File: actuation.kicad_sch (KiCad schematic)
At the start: 0 parts

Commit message: GPIO, ADC
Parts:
- added U?: TLI4971, Package_SON:Infineon_PG-TISON-8-5, symbol actuation:TLI4971
- added U?: PCA9615, Package_SO:TSSOP-10_3x3mm_P0.5mm, symbol actuation:PCA9615
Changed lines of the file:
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@@
 (kicad_sch (version 20211123) (generator eeschema)
   (paper "A4")
+  (symbol (lib_id "actuation:TLI4971") (at 41.91 107.95 0) (unit 1)
+    (in_bom yes) (on_board yes) (fields_autoplaced)
+    (property "Reference" "U?" (id 0) (at 42.545 101.6 0))
+    (property "Value" "TLI4971" (id 1) (at 42.545 104.14 0))
+    (property "Footprint" "Package_SON:Infineon_PG-TISON-8-5" (id 2) (at 44.45 125.73 0)
+      (effects (font (size 1.27 1.27)) hide)
+    )
+    (property "Datasheet" "https://www.infineon.com/dgdl/Infineon-TLI4971_25_50_75_120-DataSheet-v01_20-EN.pdf?fileId=5546d462700c0ae6017034d731621b09" (id 3) (at 40.64 128.27 0)
+      (effects (font (size 1.27 1.27)) hide)
+    )
+    (property "MPN" "TLI4971A050T5UE0001XUMA1" (id 4) (at 44.45 123.19 0)
+      (effects (font (size 1.27 1.27)) hide)
+    )
+    (pin "1")
+    (pin "2")
+    (pin "3")
+    (pin "4")
+    (pin "5")
+    (pin "6")
+    (pin "7")
+    (pin "8")
+  )
+  (symbol (lib_id "actuation:PCA9615") (at 45.72 64.77 0) (unit 1)
+    (in_bom yes) (on_board yes) (fields_autoplaced)
+    (property "Reference" "U?" (id 0) (at 45.72 59.69 0))
+    (property "Value" "PCA9615" (id 1) (at 45.72 62.23 0))
+    (property "Footprint" "Package_SO:TSSOP-10_3x3mm_P0.5mm" (id 2) (at 45.72 90.17 0)
+      (effects (font (size 1.27 1.27)) hide)
+    )
+    (property "Datasheet" "https://www.nxp.com/docs/en/data-sheet/PCA9615.pdf" (id 3) (at 46.99 95.25 0)
+      (effects (font (size 1.27 1.27)) hide)
+    )
+    (property "MPN" "PCA9615DPZ" (id 4) (at 45.72 92.71 0)
+      (effects (font (size 1.27 1.27)) hide)
+    )
+    (pin "1")
+    (pin "10")
+    (pin "2")
+    (pin "3")
+    (pin "4")
+    (pin "5")
+    (pin "6")
+    (pin "7")
+    (pin "8")
+    (pin "9")
+  )
   (sheet_instances
     (path "/" (page "1"))
   )
+  (symbol_instances
+    (path "/1d4e175b-070d-4ba2-acb6-e76800f88675"
+      (reference "U?") (unit 1) (value "TLI4971") (footprint "Package_SON:Infineon_PG-TISON-8-5")
+    )
+    (path "/b052b9a3-1f94-4103-824a-f8b60996bb3f"
+      (reference "U?") (unit 1) (value "PCA9615") (footprint "Package_SO:TSSOP-10_3x3mm_P0.5mm")
+    )
+  )
 )

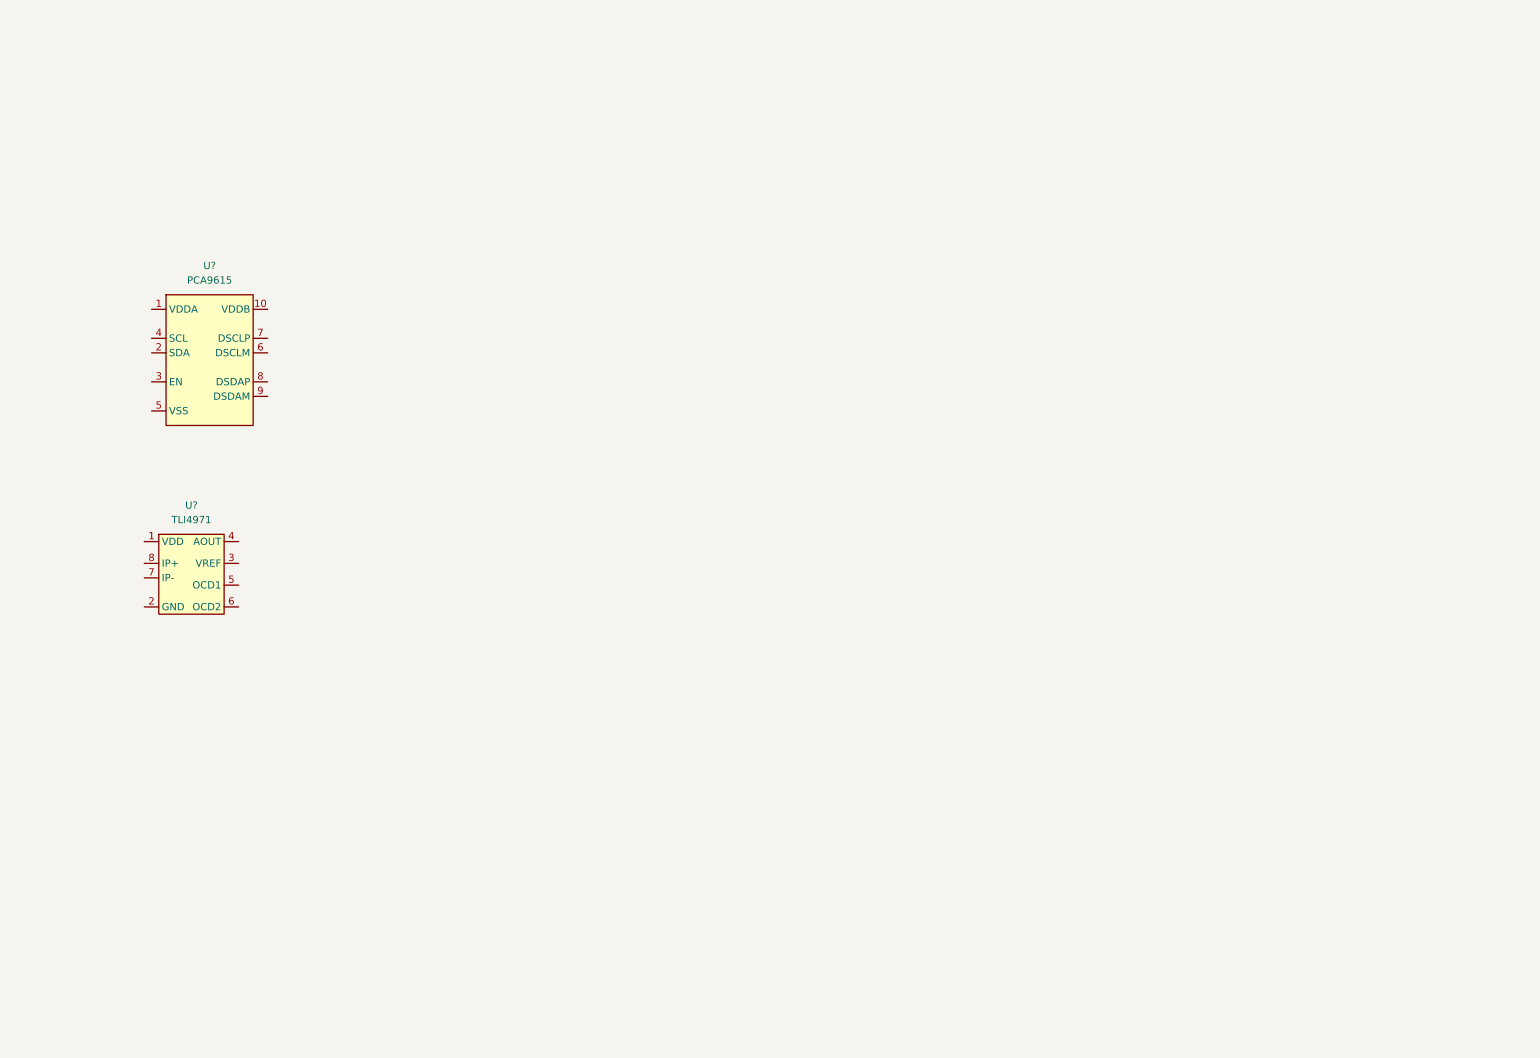
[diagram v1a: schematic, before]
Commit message: made symbols for ssr, optocoupler (missing footprint)
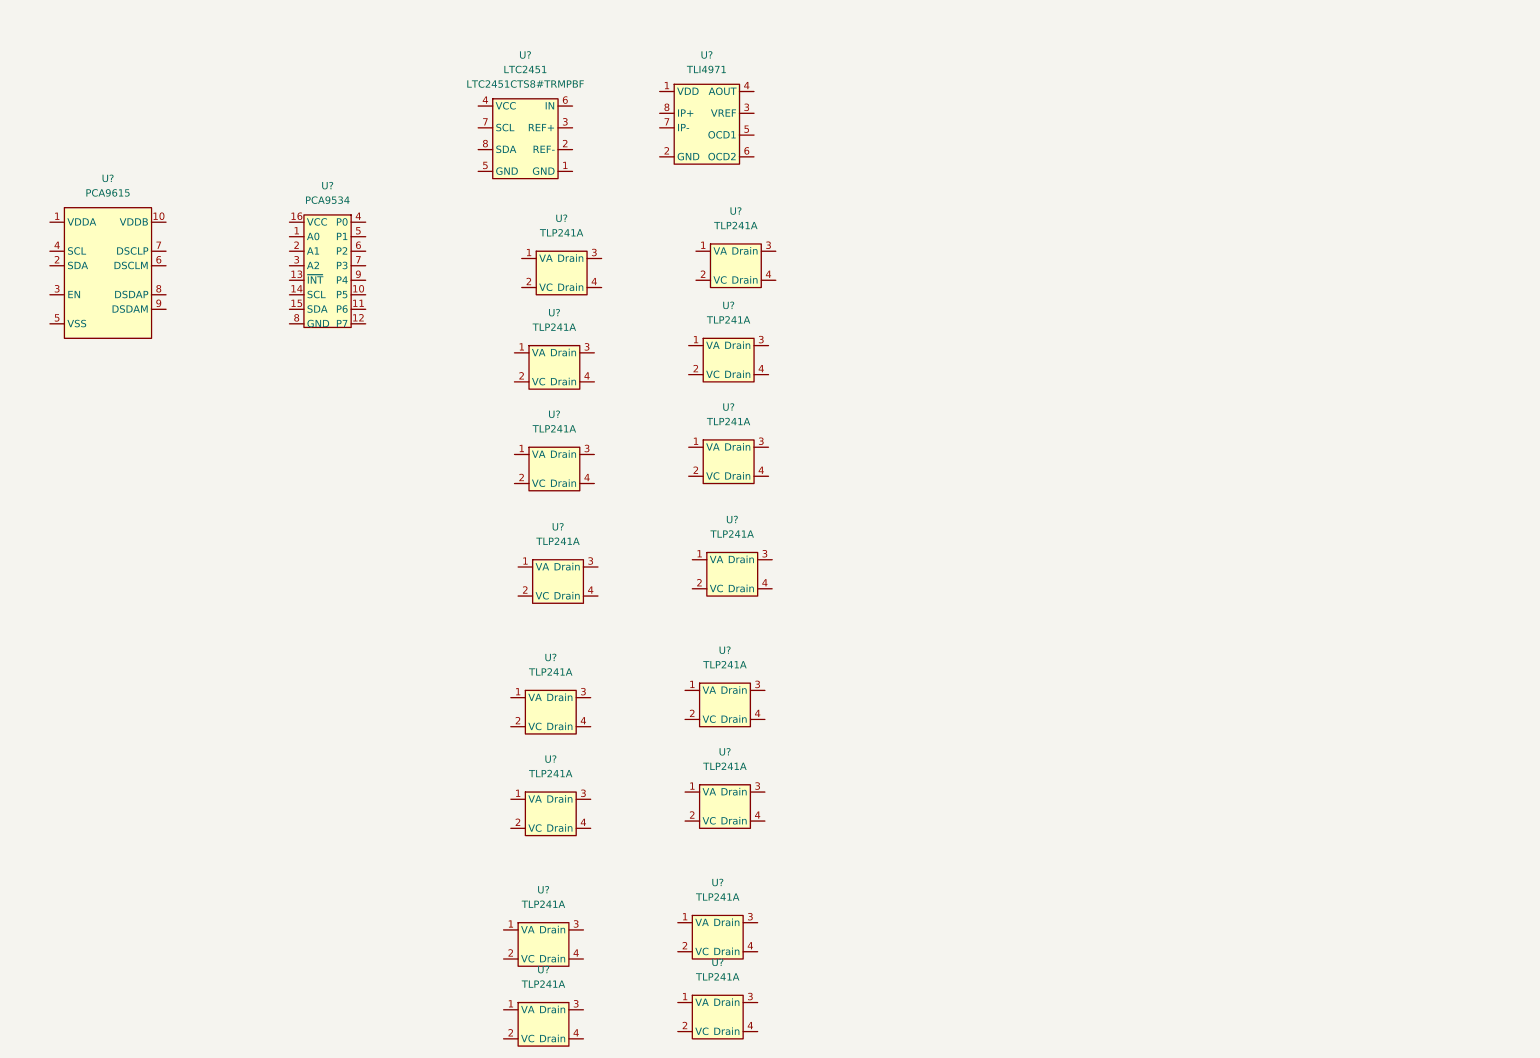
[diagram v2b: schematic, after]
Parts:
- added U? (x16): TLP241A, symbol actuation:TLP241A
- added U?: LTC2451, Package_TO_SOT_SMD:TSOT-23-8, symbol actuation:LTC2451
- added U?: PCA9534, Package_SO:TSSOP-16_4.4x5mm_P0.65mm, symbol actuation:PCA9534
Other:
- moved on the sheet: U?
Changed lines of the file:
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@@
 (kicad_sch (version 20211123) (generator eeschema)
   (paper "A4")
-  (symbol (lib_id "actuation:TLI4971") (at 41.91 107.95 0) (unit 1)
-    (in_bom yes) (on_board yes) (fields_autoplaced)
-    (property "Reference" "U?" (id 0) (at 42.545 101.6 0))
-    (property "Value" "TLI4971" (id 1) (at 42.545 104.14 0))
-    (property "Footprint" "Package_SON:Infineon_PG-TISON-8-5" (id 2) (at 44.45 125.73 0)
-      (effects (font (size 1.27 1.27)) hide)
-    )
-    (property "Datasheet" "https://www.infineon.com/dgdl/Infineon-TLI4971_25_50_75_120-DataSheet-v01_20-EN.pdf?fileId=5546d462700c0ae6017034d731621b09" (id 3) (at 40.64 128.27 0)
-      (effects (font (size 1.27 1.27)) hide)
-    )
-    (property "MPN" "TLI4971A050T5UE0001XUMA1" (id 4) (at 44.45 123.19 0)
-      (effects (font (size 1.27 1.27)) hide)
-    )
-    (pin "1")
-    (pin "2")
-    (pin "3")
-    (pin "4")
-    (pin "5")
-    (pin "6")
-    (pin "7")
-    (pin "8")
-  )
-  (symbol (lib_id "actuation:PCA9615") (at 45.72 64.77 0) (unit 1)
-    (in_bom yes) (on_board yes) (fields_autoplaced)
-    (property "Reference" "U?" (id 0) (at 45.72 59.69 0))
-    (property "Value" "PCA9615" (id 1) (at 45.72 62.23 0))
-    (property "Footprint" "Package_SO:TSSOP-10_3x3mm_P0.5mm" (id 2) (at 45.72 90.17 0)
-      (effects (font (size 1.27 1.27)) hide)
-    )
-    (property "Datasheet" "https://www.nxp.com/docs/en/data-sheet/PCA9615.pdf" (id 3) (at 46.99 95.25 0)
-      (effects (font (size 1.27 1.27)) hide)
-    )
-    (property "MPN" "PCA9615DPZ" (id 4) (at 45.72 92.71 0)
-      (effects (font (size 1.27 1.27)) hide)
-    )
-    (pin "1")
-    (pin "10")
-    (pin "2")
-    (pin "3")
-    (pin "4")
-    (pin "5")
-    (pin "6")
-    (pin "7")
-    (pin "8")
-    (pin "9")
-  )
-  (sheet_instances
-    (path "/" (page "1"))
-  )
-  (symbol_instances
-    (path "/1d4e175b-070d-4ba2-acb6-e76800f88675"
-      (reference "U?") (unit 1) (value "TLI4971") (footprint "Package_SON:Infineon_PG-TISON-8-5")
-    )
-    (path "/b052b9a3-1f94-4103-824a-f8b60996bb3f"
-      (reference "U?") (unit 1) (value "PCA9615") (footprint "Package_SO:TSSOP-10_3x3mm_P0.5mm")
-    )
-  )
-)

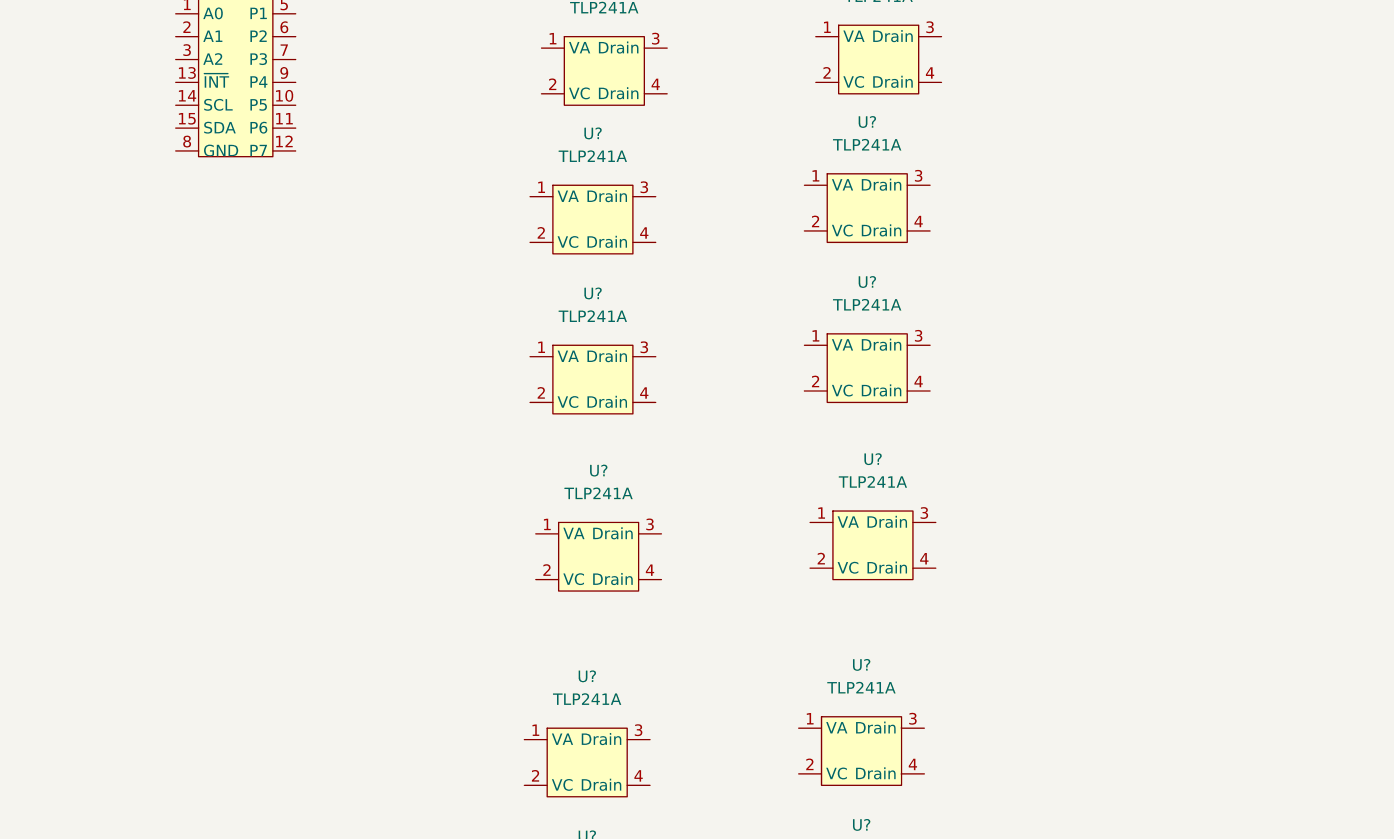
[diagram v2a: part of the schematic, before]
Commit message: Finished optocoupler, and ssr
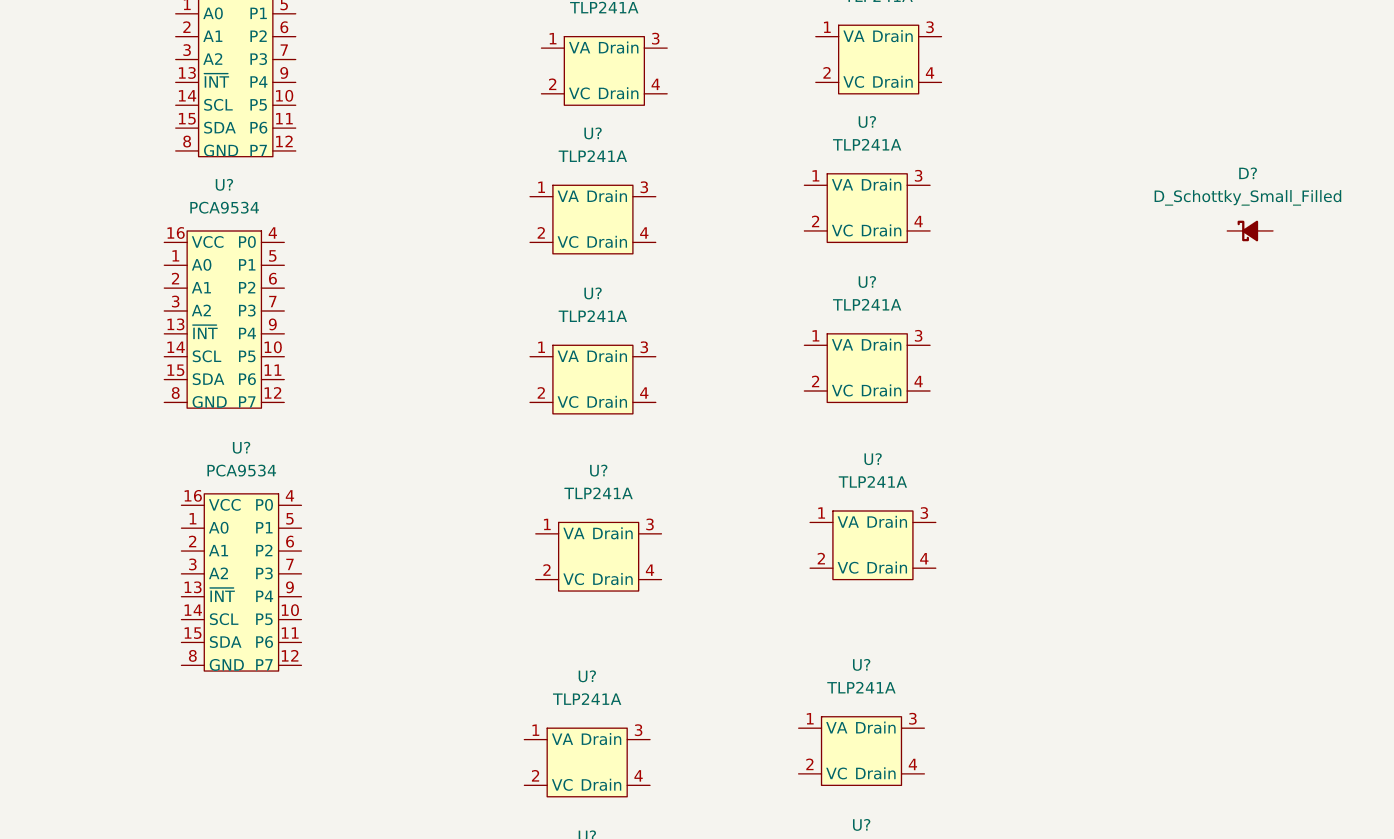
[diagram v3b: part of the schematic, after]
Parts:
- added D?: D_Schottky_Small_Filled, Diode_SMD:D_SMA, symbol Device:D_Schottky_Small_Filled
- added U? (x2): PCA9534, Package_SO:TSSOP-16_4.4x5mm_P0.65mm, symbol actuation:PCA9534
